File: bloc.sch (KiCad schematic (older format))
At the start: 11 parts, among them U1 TPIC6C595, U2 KCSA02-106

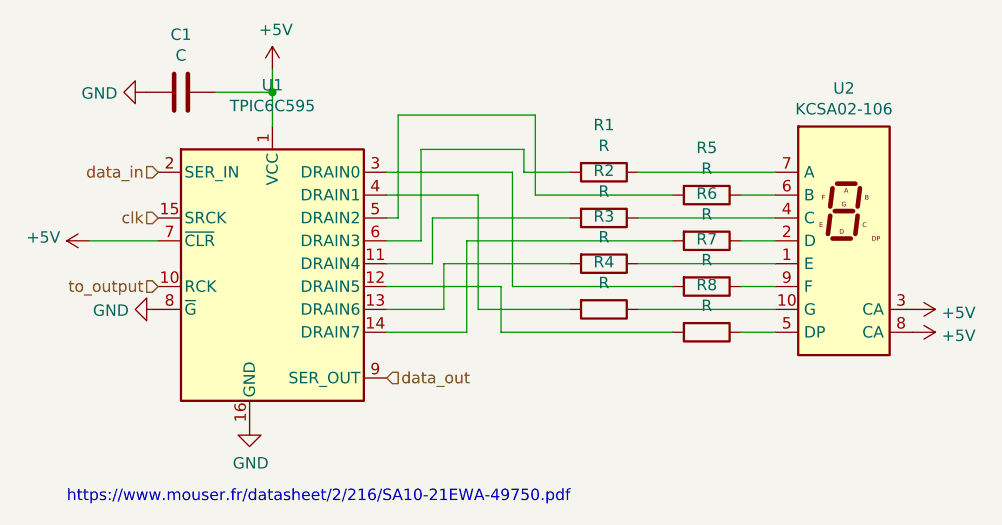
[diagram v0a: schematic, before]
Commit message: with cms resistors
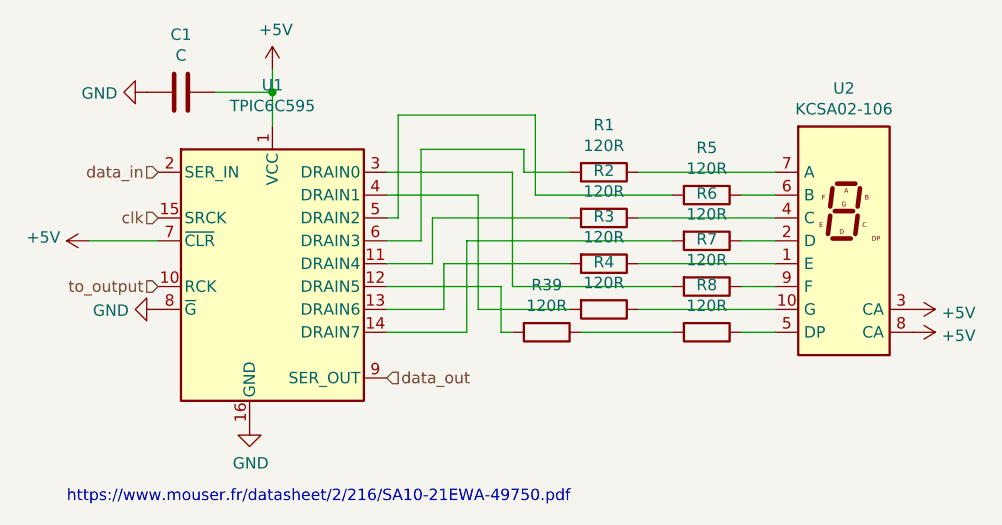
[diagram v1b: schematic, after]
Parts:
- added R39: 120R, Resistor_SMD:R_0805_2012Metric_Pad1.20x1.40mm_HandSolder, symbol Device:R
- R1, R2, R3, R4, R5, R6, R7, R8: value R -> 120R; footprint Resistor_THT:R_Axial_DIN0207_L6.3mm_D2.5mm_P7.62mm_Horizontal -> Resistor_SMD:R_0805_2012Metric_Pad1.20x1.40mm_HandSolder
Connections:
- net at R8.2: now also R39.1; no longer U1.12 (DRAIN5)
- new net: R39.2, U1.12 (DRAIN5)
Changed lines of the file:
@@
 AR Path="/618A561D/6188E204" Ref="R32"  Part="1"
 F 0 "R8" V 4593 4000 50  0000 C CNN
-F 1 "R" V 4684 4000 50  0000 C CNN
-F 2 "Resistor_THT:R_Axial_DIN0207_L6.3mm_D2.5mm_P7.62mm_Horizontal" V 4730 4000 50  0001 C CNN
+F 1 "120R" V 4684 4000 50  0000 C CNN
+F 2 "Resistor_SMD:R_0805_2012Metric_Pad1.20x1.40mm_HandSolder" V 4730 4000 50  0001 C CNN
 F 3 "~" H 4800 4000 50  0001 C CNN
 	1    4800 4000
@@
 AR Path="/618A561D/6188E1FE" Ref="R28"  Part="1"
 F 0 "R4" V 4143 3900 50  0000 C CNN
-F 1 "R" V 4234 3900 50  0000 C CNN
-F 2 "Resistor_THT:R_Axial_DIN0207_L6.3mm_D2.5mm_P7.62mm_Horizontal" V 4280 3900 50  0001 C CNN
+F 1 "120R" V 4234 3900 50  0000 C CNN
+F 2 "Resistor_SMD:R_0805_2012Metric_Pad1.20x1.40mm_HandSolder" V 4280 3900 50  0001 C CNN
 F 3 "~" H 4350 3900 50  0001 C CNN
 	1    4350 3900
@@
 AR Path="/618A561D/6188DD80" Ref="R31"  Part="1"
 F 0 "R7" V 4593 3800 50  0000 C CNN
-F 1 "R" V 4684 3800 50  0000 C CNN
-F 2 "Resistor_THT:R_Axial_DIN0207_L6.3mm_D2.5mm_P7.62mm_Horizontal" V 4730 3800 50  0001 C CNN
+F 1 "120R" V 4684 3800 50  0000 C CNN
+F 2 "Resistor_SMD:R_0805_2012Metric_Pad1.20x1.40mm_HandSolder" V 4730 3800 50  0001 C CNN
 F 3 "~" H 4800 3800 50  0001 C CNN
 	1    4800 3800
@@
 AR Path="/618A561D/6188DD7A" Ref="R27"  Part="1"
 F 0 "R3" V 4143 3700 50  0000 C CNN
-F 1 "R" V 4234 3700 50  0000 C CNN
-F 2 "Resistor_THT:R_Axial_DIN0207_L6.3mm_D2.5mm_P7.62mm_Horizontal" V 4280 3700 50  0001 C CNN
+F 1 "120R" V 4234 3700 50  0000 C CNN
+F 2 "Resistor_SMD:R_0805_2012Metric_Pad1.20x1.40mm_HandSolder" V 4280 3700 50  0001 C CNN
 F 3 "~" H 4350 3700 50  0001 C CNN
 	1    4350 3700
@@
 AR Path="/618A561D/6188D8E8" Ref="R30"  Part="1"
 F 0 "R6" V 4593 3600 50  0000 C CNN
-F 1 "R" V 4684 3600 50  0000 C CNN
-F 2 "Resistor_THT:R_Axial_DIN0207_L6.3mm_D2.5mm_P7.62mm_Horizontal" V 4730 3600 50  0001 C CNN
+F 1 "120R" V 4684 3600 50  0000 C CNN
+F 2 "Resistor_SMD:R_0805_2012Metric_Pad1.20x1.40mm_HandSolder" V 4730 3600 50  0001 C CNN
 F 3 "~" H 4800 3600 50  0001 C CNN
 	1    4800 3600
@@
 AR Path="/618A561D/6188D8E2" Ref="R26"  Part="1"
 F 0 "R2" V 4143 3500 50  0000 C CNN
-F 1 "R" V 4234 3500 50  0000 C CNN
-F 2 "Resistor_THT:R_Axial_DIN0207_L6.3mm_D2.5mm_P7.62mm_Horizontal" V 4280 3500 50  0001 C CNN
+F 1 "120R" V 4234 3500 50  0000 C CNN
+F 2 "Resistor_SMD:R_0805_2012Metric_Pad1.20x1.40mm_HandSolder" V 4280 3500 50  0001 C CNN
 F 3 "~" H 4350 3500 50  0001 C CNN
 	1    4350 3500
@@
 AR Path="/618A561D/6188D18D" Ref="R29"  Part="1"
 F 0 "R5" V 4593 3400 50  0000 C CNN
-F 1 "R" V 4684 3400 50  0000 C CNN
-F 2 "Resistor_THT:R_Axial_DIN0207_L6.3mm_D2.5mm_P7.62mm_Horizontal" V 4730 3400 50  0001 C CNN
+F 1 "120R" V 4684 3400 50  0000 C CNN
+F 2 "Resistor_SMD:R_0805_2012Metric_Pad1.20x1.40mm_HandSolder" V 4730 3400 50  0001 C CNN
 F 3 "~" H 4800 3400 50  0001 C CNN
 	1    4800 3400
@@
 AR Path="/618A561D/6188CBCD" Ref="R25"  Part="1"
 F 0 "R1" V 4143 3300 50  0000 C CNN
-F 1 "R" V 4234 3300 50  0000 C CNN
-F 2 "Resistor_THT:R_Axial_DIN0207_L6.3mm_D2.5mm_P7.62mm_Horizontal" V 4280 3300 50  0001 C CNN
+F 1 "120R" V 4234 3300 50  0000 C CNN
+F 2 "Resistor_SMD:R_0805_2012Metric_Pad1.20x1.40mm_HandSolder" V 4280 3300 50  0001 C CNN
 F 3 "~" H 4350 3300 50  0001 C CNN
 	1    4350 3300
@@
 	3900 3800 3900 4000
 Wire Wire Line
-	3900 4000 4650 4000
-Wire Wire Line
 	3400 3800 3900 3800
 Wire Wire Line
@@
 	0    1    1    0
 $EndComp
+$Comp
+L Device:R R?
+U 1 1 61918DC2
+P 4100 4000
+AR Path="/61884464/61918DC2" Ref="R?"  Part="1"
+AR Path="/618A5117/61918DC2" Ref="R39"  Part="1"
+AR Path="/618A51E6/61918DC2" Ref="R40"  Part="1"
+AR Path="/618A54D1/61918DC2" Ref="R41"  Part="1"
+AR Path="/618A561D/61918DC2" Ref="R42"  Part="1"
+F 0 "R39" V 3893 4000 50  0000 C CNN
+F 1 "120R" V 3984 4000 50  0000 C CNN
+F 2 "Resistor_SMD:R_0805_2012Metric_Pad1.20x1.40mm_HandSolder" V 4030 4000 50  0001 C CNN
+F 3 "~" H 4100 4000 50  0001 C CNN
+	1    4100 4000
+	0    1    1    0
+$EndComp
+Wire Wire Line
+	3900 4000 3950 4000
+Wire Wire Line
+	4250 4000 4650 4000
 $EndSCHEMATC
